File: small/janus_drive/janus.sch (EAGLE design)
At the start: 27 parts, among them IC1 LM741

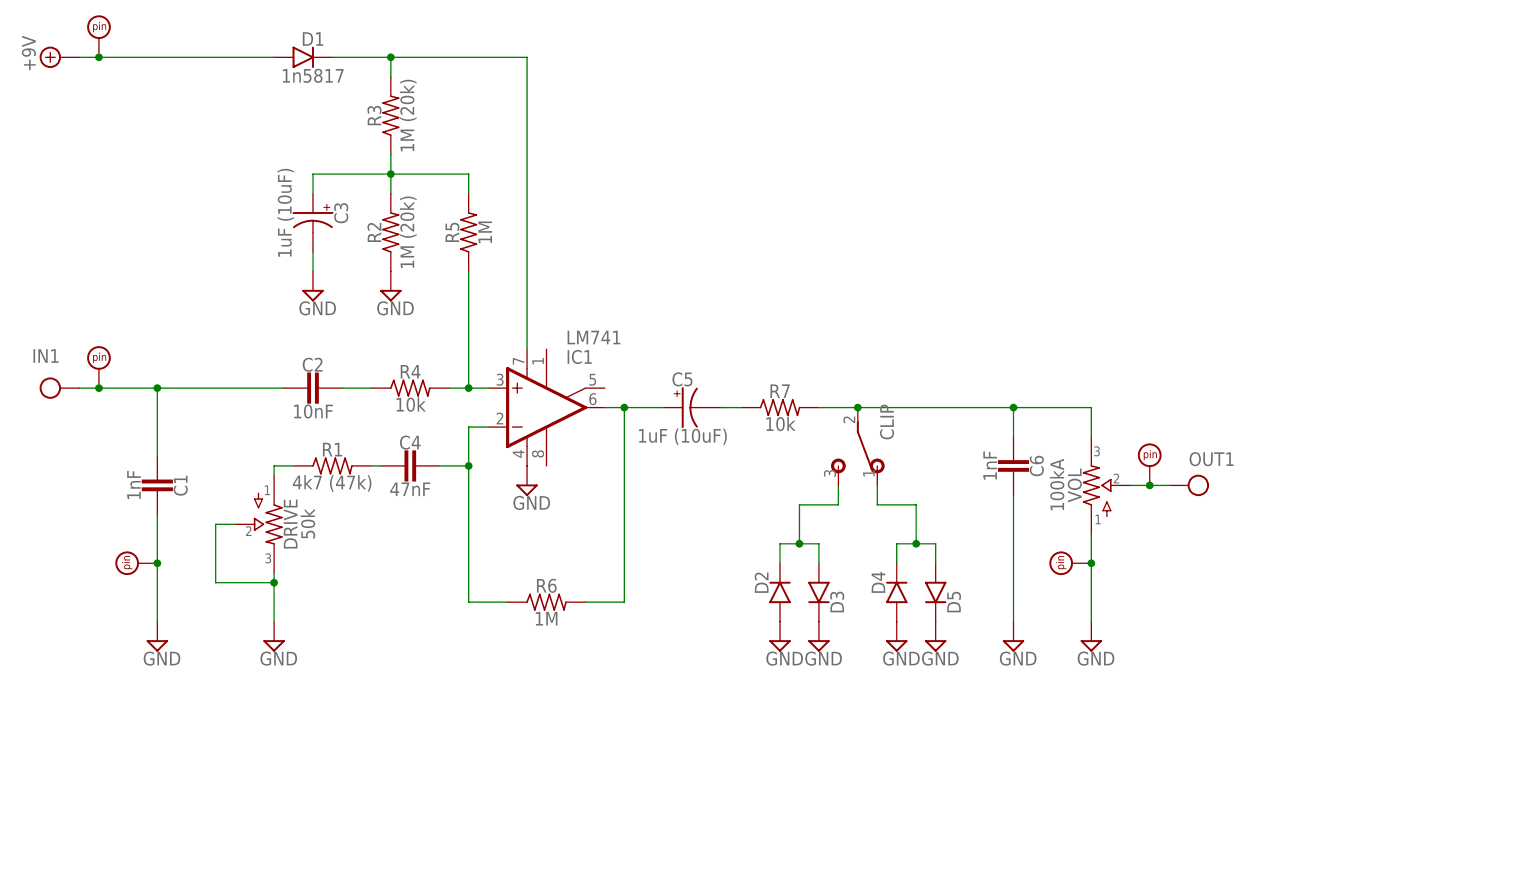
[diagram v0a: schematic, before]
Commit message: updated Gaius Ringer & Janus Drive, added Chimera Chorus
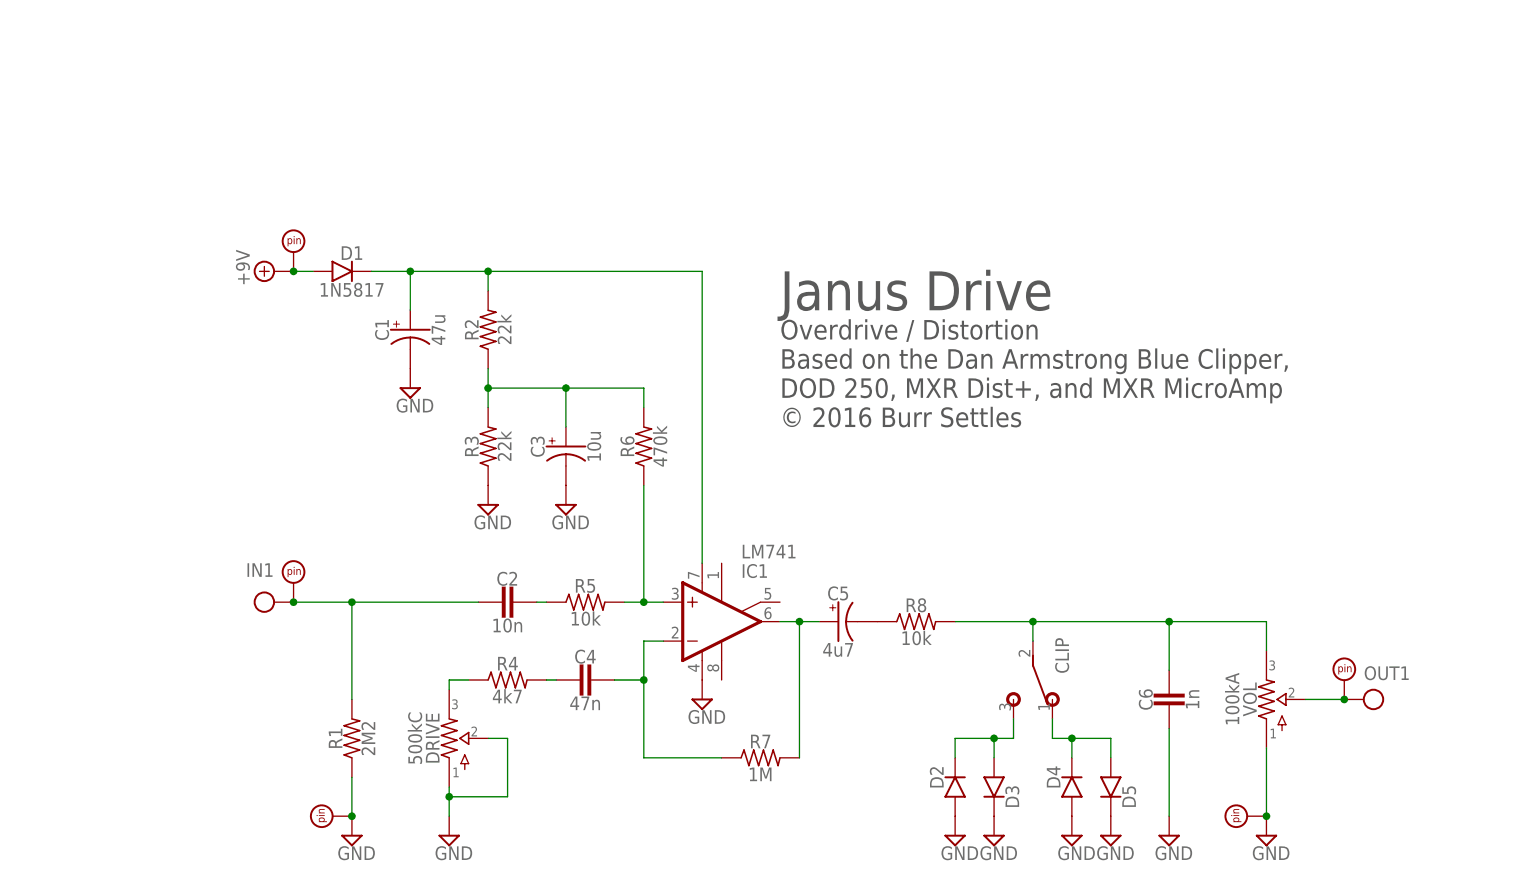
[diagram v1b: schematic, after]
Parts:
- added R8: 10k, resistors:R_.3B
- C1: value 1nF -> 47u; device capacitors-film:CER/FILMBOX.1 -> capacitors-elec:0501
- C2: value 10nF -> 10n
- C3: value 1uF (10uF) -> 10u
- C4: value 47nF -> 47n
- C5: value 1uF (10uF) -> 4u7
- C6: value 1nF -> 1n
- D1: value 1n5817 -> 1N5817
- D4, D5: device diodes:DO35.2 -> diodes:DO35.3
- DRIVE: value 50k -> 500kC; device potentiometers:POTSTRIM -> potentiometers:POTSSMALL_PADS
- R1: value 4k7 (47k) -> 2M2
- R2, R3: value 1M (20k) -> 22k
- R4: value 10k -> 4k7
- R5: value 1M -> 10k
- R6: value 1M -> 470k
- R7: value 10k -> 1M
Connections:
- net +9V: now also PAD1.P$1; no longer PAD2.P$1
- net CLIP: now also R8.2; no longer R7.2
- net GND: now also C1.-, DRIVE.1, R1.1, R3.1; no longer C1.1, DRIVE.3, R2.1
- net IN: now also PAD2.P$1, R1.2; no longer C1.2, PAD1.P$1
- net N$1: now also R5.1; no longer R4.1
- net N$10: now also DRIVE.3, R4.1; no longer DRIVE.1, R1.1
- net N$12: now also C1.+, R2.2; no longer R3.2
- net N$2: now also R5.2, R6.1; no longer R4.2, R5.1
- net N$3: now also R7.1; no longer R6.1
- net N$4: now also R4.2; no longer R1.2
- net N$5: now also R7.2; no longer R6.2
- net N$6: now also R8.1; no longer R7.1
- net N$8: now also R2.1, R3.2, R6.2; no longer R2.2, R3.1, R5.2
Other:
- note added: "Janus Drive"
- note added: "Overdrive / Distortion Based on the Dan Armstrong Blue Clipper, DOD 250, MXR Dist+, and MXR MicroAmp © 2016 Burr Settles"
- moved on the sheet: C2, C3, C4, C5, C6, CLIP, D1, D2, D3, D4, D5, DRIVE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

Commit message: updates to a few small pedals
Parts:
- removed VOL: 100kA, potentiometers:POTSSMALL_PADS
- added VOLUME: 100kA, potentiometers:POTSSMALL_PADS
- C1: value 47u -> 2n2; device capacitors-elec:0501 -> capacitors-film:CER/FILMBOX.1
- C2: value 10n -> 47u; device capacitors-film:CER/FILMBOX.1 -> capacitors-elec:0501
- C3: value 10u -> 10n; device capacitors-elec:0501 -> capacitors-film:CER/FILMBOX.1
- C4: value 47n -> 10u; device capacitors-film:CER/FILMBOX.1 -> capacitors-elec:0501
- C5: value 4u7 -> 47n; device capacitors-elec:0501 -> capacitors-film:CER/FILMBOX.1
- C6: value 1n -> 4u7; device capacitors-film:CER/FILMBOX.1 -> capacitors-elec:0501
- R1: value 2M2 -> 1M
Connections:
- net CLIP: now also VOLUME.3; no longer C6.2, VOL.3
- net GND: now also C1.1, C2.-, C4.-, VOLUME.1; no longer C1.-, C3.-, C6.1, VOL.1
- net IN: now also C1.2, C3.2; no longer C2.2
- net N$1: now also C3.1; no longer C2.1
- net N$12: now also C2.+; no longer C1.+
- net N$3: now also C5.1; no longer C4.1
- net N$4: now also C5.2; no longer C4.2
- net N$5: now also C6.+; no longer C5.+
- net N$6: now also C6.-; no longer C5.-
- net N$8: now also C4.+; no longer C3.+
- net OUT: now also VOLUME.2; no longer VOL.2
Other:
- note added: "JANUS DRIVE"
- note added: "OVERDRIVE / DISTORTION mashup of the Dan Armstrong Blue Clipper, MXR Dist+, DOD 250, and MXR MicroAmp © 2016 burr settles"
- note removed: "Janus Drive"
- note removed: "Overdrive / Distortion Based on the Dan Armstrong Blue Clipper, DOD 250, MXR Dist+, and MXR MicroAmp © 2016 Burr Settles"
- moved on the sheet: CLIP, D2, D3, D4, D5, DRIVE, IC1, R1, R2, R3, R4, R5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

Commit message: formatting updates
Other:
- note added: "OVERDRIVE / DISTORTION mashup of the dan armstrong blue clipper, mxr dist+, dod 250, and mxr microamp (c) 2016 burr settles"
- note removed: "OVERDRIVE / DISTORTION mashup of the Dan Armstrong Blue Clipper, MXR Dist+, DOD 250, and MXR MicroAmp © 2016 burr settles"
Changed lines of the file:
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@@
 <sheet>
 <plain>
-<text x="78.74" y="76.2" size="5.08" layer="97">JANUS DRIVE</text>
-<text x="78.74" y="60.96" size="2.54" layer="97">OVERDRIVE / DISTORTION
-mashup of the Dan Armstrong Blue Clipper,
-MXR Dist+, DOD 250, and MXR MicroAmp
-© 2016 burr settles</text>
+<text x="78.74" y="73.66" size="6.4516" layer="97">JANUS DRIVE</text>
+<text x="78.74" y="60.96" size="1.9304" layer="97">OVERDRIVE / DISTORTION
+mashup of the dan armstrong blue clipper,
+mxr dist+, dod 250, and mxr microamp
+(c) 2016 burr settles</text>
 </plain>
 <instances>
